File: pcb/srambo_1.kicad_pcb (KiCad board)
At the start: 2 copper layers, 113 x 42 mm, 29 parts, among them P1 JTAG, P10 EMMU_LEFT, P11 MMU_LEFT, P12 DRAM_RIGHT, P13 EMMU_RIGHT, P14 MMU_RIGHT, P2 GND, P3 AUX_B, P4 AUX_A, P5 DATA5-7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

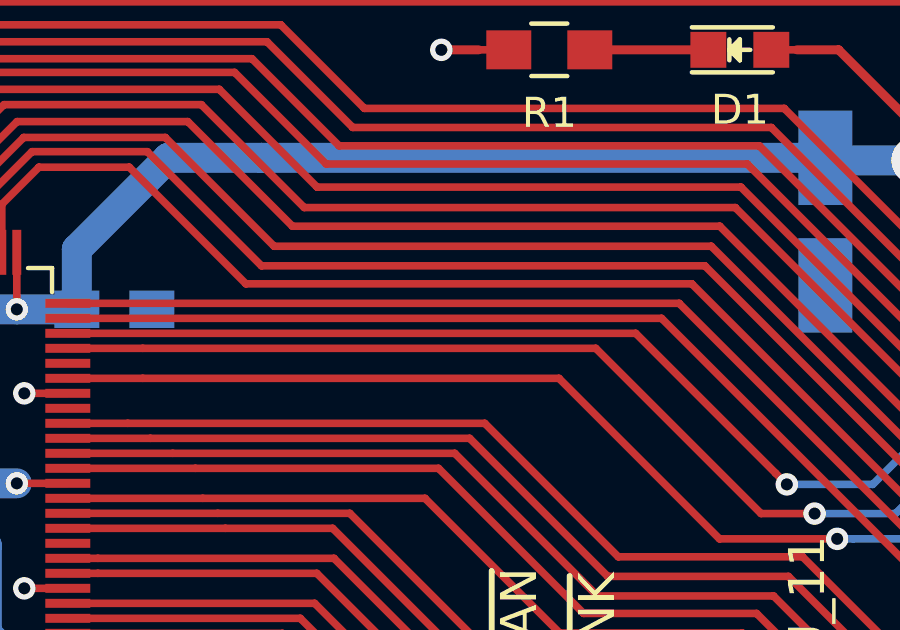
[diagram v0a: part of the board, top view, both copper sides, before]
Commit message: PCB: Add OSHW logo
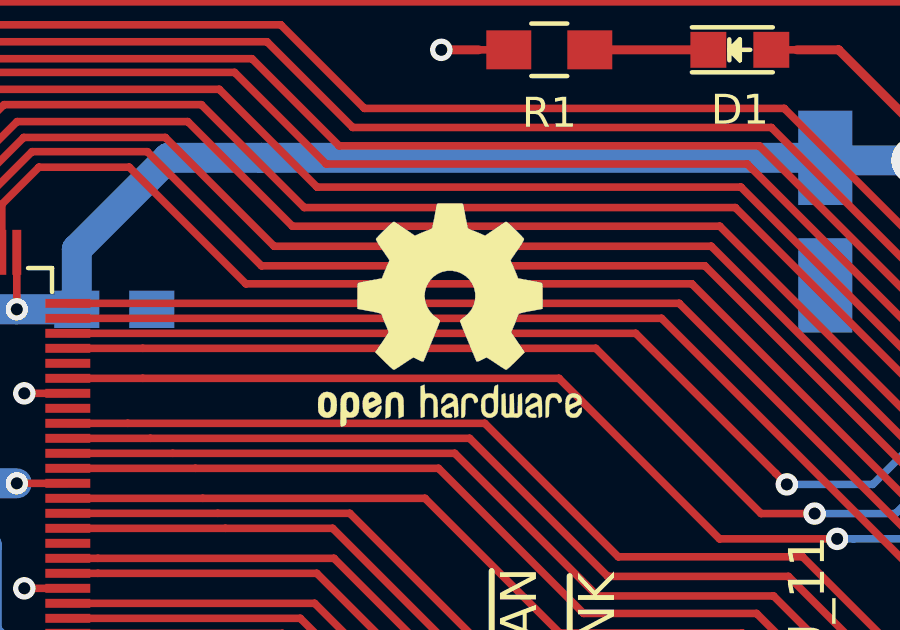
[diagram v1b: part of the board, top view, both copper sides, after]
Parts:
- added REF***: OSHW-Logo2_9.8x8mm_SilkScreen, Symbols:OSHW-Logo2_9.8x8mm_SilkScreen, F.Cu at (109.7, 61.4)
